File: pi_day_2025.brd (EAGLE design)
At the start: 50.8 x 25.4 mm, 98 parts, among them IC1 W25Q64JVXGIQ, J4 SM03B-SRSS-TB(LF)(SN), Q2 310mA/60V/1.6Ω, U1 APS6404L-3SQR-ZR, U2 RP2350A, U3 TPS76318DBVRG4, U4 TPS63001DRCR, U5 TXS0108EPWRG4, U6 LSM6DS3TR-C, U7 MCP73833T-AMI/MF, U8 TPS2113APWR, Y1 12MHz

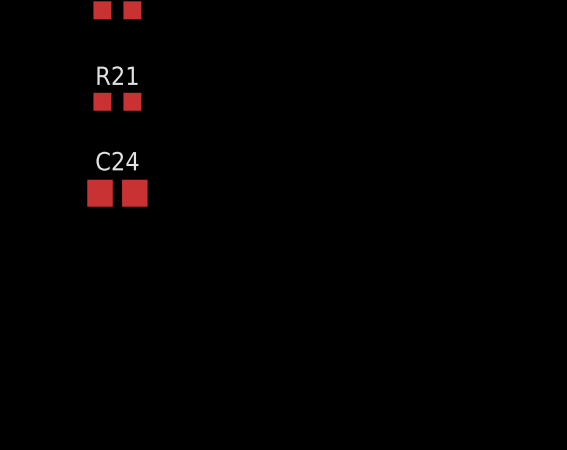
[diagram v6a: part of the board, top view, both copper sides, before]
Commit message: Added 1.8V regulator
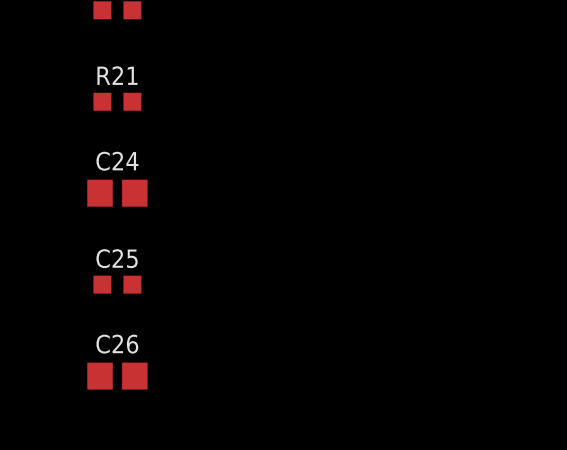
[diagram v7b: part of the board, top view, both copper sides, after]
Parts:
- added C25: 4.7uF, SparkFun-Capacitors:0402-TIGHT
- added C26: 1.0uF, SparkFun-Capacitors:0402
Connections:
- net 1.8V: now also C25.1, U3.5
- net 3.3V: now also C26.1, U3.1, U3.3
- net GND: now also C25.2, C26.2
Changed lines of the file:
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@@
 <attribute name="VALUE" x="-75.692" y="-283.718" size="0.6096" layer="27" font="vector" ratio="20" align="top-center"/>
+</element>
+<element name="C25" library="SparkFun-Capacitors" library_urn="urn:adsk.eagle:library:510" package="0402-TIGHT" package3d_urn="urn:adsk.eagle:package:41385069/1" value="4.7uF" x="-75.692" y="-286.004" smashed="yes">
+<attribute name="NAME" x="-75.692" y="-285.442" size="0.6096" layer="25" font="vector" ratio="20" align="bottom-center"/>
+<attribute name="PROD_ID" value="CAP-14240" x="-75.692" y="-286.004" size="1.778" layer="27" display="off"/>
+<attribute name="VALUE" x="-75.692" y="-286.566" size="0.6096" layer="27" font="vector" ratio="20" align="top-center"/>
+</element>
+<element name="C26" library="SparkFun-Capacitors" library_urn="urn:adsk.eagle:library:510" package="0402" package3d_urn="urn:adsk.eagle:package:41385089/1" value="1.0uF" x="-75.692" y="-289.052" smashed="yes">
+<attribute name="NAME" x="-75.692" y="-288.29" size="0.6096" layer="25" font="vector" ratio="20" align="bottom-center"/>
+<attribute name="PROD_ID" value="CAP-12417" x="-75.692" y="-289.052" size="1.778" layer="27" display="off"/>
+<attribute name="VALUE" x="-75.692" y="-289.814" size="0.6096" layer="27" font="vector" ratio="20" align="top-center"/>
 </element>
 </elements>
@@
 <contactref element="C23" pad="2"/>
 <contactref element="C24" pad="2"/>
+<contactref element="C25" pad="2"/>
+<contactref element="C26" pad="2"/>
 <wire x1="-47.991" y1="-197.104" x2="-50.978" y2="-197.997" width="0" layer="19" extent="1-1"/>
 <wire x1="-54.872" y1="-203.538" x2="-50.978" y2="-197.997" width="0" layer="19" extent="1-1"/>
@@
 <wire x1="-75.192" y1="-276.86" x2="-75.192" y2="-266.192" width="0" layer="19" extent="1-1"/>
 <wire x1="-75.112" y1="-282.956" x2="-75.192" y2="-276.86" width="0" layer="19" extent="1-1"/>
+<wire x1="-75.192" y1="-286.004" x2="-75.112" y2="-282.956" width="0" layer="19" extent="1-1"/>
+<wire x1="-75.112" y1="-289.052" x2="-75.192" y2="-286.004" width="0" layer="19" extent="1-1"/>
 <wire x1="-16.903" y1="-171.45" x2="-39.869" y2="-197.836" width="0" layer="19" extent="1-1"/>
 <wire x1="-17.708" y1="-157.48" x2="-16.903" y2="-171.45" width="0" layer="19" extent="1-1"/>
@@
 <contactref element="C21" pad="1"/>
 <contactref element="C22" pad="1"/>
-<wire x1="-54.022" y1="-203.188" x2="-35.462" y2="-198.374" width="0" layer="19" extent="1-1"/>
-<wire x1="-55.872" y1="-203.538" x2="-54.022" y2="-203.188" width="0" layer="19" extent="1-1"/>
-<wire x1="-56.722" y1="-201.688" x2="-55.872" y2="-203.538" width="0" layer="19" extent="1-1"/>
-<wire x1="-54.872" y1="-201.338" x2="-56.722" y2="-201.688" width="0" layer="19" extent="1-1"/>
+<contactref element="U3" pad="1"/>
+<contactref element="U3" pad="3"/>
+<contactref element="C26" pad="1"/>
+<wire x1="-47.991" y1="-198.054" x2="-47.991" y2="-196.154" width="0" layer="19" extent="1-1"/>
+<wire x1="-54.872" y1="-201.338" x2="-47.991" y2="-198.054" width="0" layer="19" extent="1-1"/>
+<wire x1="-56.722" y1="-201.688" x2="-54.872" y2="-201.338" width="0" layer="19" extent="1-1"/>
+<wire x1="-55.872" y1="-203.538" x2="-56.722" y2="-201.688" width="0" layer="19" extent="1-1"/>
+<wire x1="-54.022" y1="-203.188" x2="-55.872" y2="-203.538" width="0" layer="19" extent="1-1"/>
 <wire x1="-56.888" y1="-205.74" x2="-55.872" y2="-203.538" width="0" layer="19" extent="1-1"/>
 <wire x1="-59.56" y1="-202.962" x2="-56.722" y2="-201.688" width="0" layer="19" extent="1-1"/>
 <wire x1="-62.36" y1="-202.962" x2="-59.56" y2="-202.962" width="0" layer="19" extent="1-1"/>
+<wire x1="-35.462" y1="-198.374" x2="-47.991" y2="-198.054" width="0" layer="19" extent="1-1"/>
 <wire x1="-18.868" y1="-157.48" x2="-35.462" y2="-198.374" width="0" layer="19" extent="1-1"/>
 <wire x1="-12.132" y1="-150.126" x2="-18.868" y2="-157.48" width="0" layer="19" extent="1-1"/>
@@
 <wire x1="-76.192" y1="-263.144" x2="-56.888" y2="-205.74" width="0" layer="19" extent="1-1"/>
 <wire x1="-76.192" y1="-266.192" x2="-76.192" y2="-263.144" width="0" layer="19" extent="1-1"/>
+<wire x1="-76.272" y1="-289.052" x2="-76.192" y2="-266.192" width="0" layer="19" extent="1-1"/>
 </signal>
 <signal name="!RESET">
@@
 <signal name="1.8V">
 <contactref element="MK1" pad="1"/>
+<contactref element="U3" pad="5"/>
+<contactref element="C25" pad="1"/>
+<wire x1="-39.869" y1="-195.539" x2="-45.481" y2="-196.154" width="0" layer="19" extent="1-1"/>
+<wire x1="-76.192" y1="-286.004" x2="-45.481" y2="-196.154" width="0" layer="19" extent="1-1"/>
 </signal>
 <signal name="VCCA">

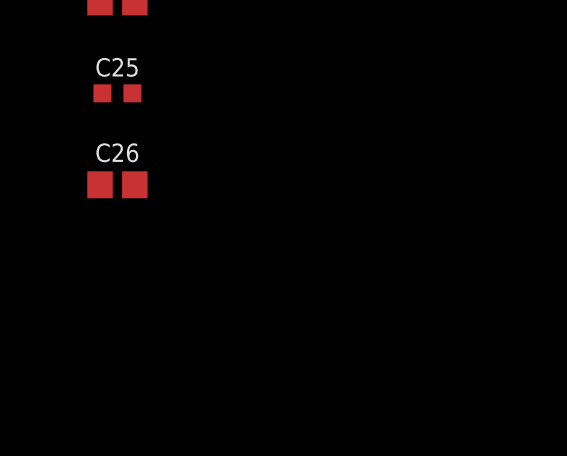
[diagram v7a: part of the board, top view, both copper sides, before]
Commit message: Added bypass capacitor to IA611
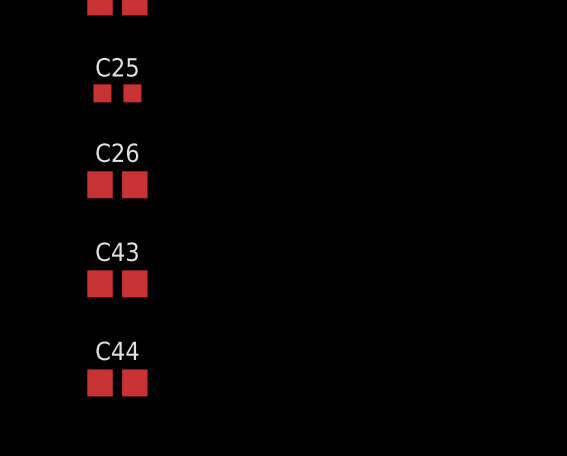
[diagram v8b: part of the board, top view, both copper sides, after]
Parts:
- added C43, C44: 1.0uF, SparkFun-Capacitors:0402
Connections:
- new net N$23: C44.1, MK1.2
- net 1.8V: now also C43.1
- net GND: now also C43.2, C44.2
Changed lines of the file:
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@@
 <attribute name="VALUE" x="-75.692" y="-289.814" size="0.6096" layer="27" font="vector" ratio="20" align="top-center"/>
+</element>
+<element name="C43" library="SparkFun-Capacitors" library_urn="urn:adsk.eagle:library:510" package="0402" package3d_urn="urn:adsk.eagle:package:41385089/1" value="1.0uF" x="-75.692" y="-292.354" smashed="yes">
+<attribute name="NAME" x="-75.692" y="-291.592" size="0.6096" layer="25" font="vector" ratio="20" align="bottom-center"/>
+<attribute name="PROD_ID" value="CAP-12417" x="-75.692" y="-292.354" size="1.778" layer="27" display="off"/>
+<attribute name="VALUE" x="-75.692" y="-293.116" size="0.6096" layer="27" font="vector" ratio="20" align="top-center"/>
+</element>
+<element name="C44" library="SparkFun-Capacitors" library_urn="urn:adsk.eagle:library:510" package="0402" package3d_urn="urn:adsk.eagle:package:41385089/1" value="1.0uF" x="-75.692" y="-295.656" smashed="yes">
+<attribute name="NAME" x="-75.692" y="-294.894" size="0.6096" layer="25" font="vector" ratio="20" align="bottom-center"/>
+<attribute name="PROD_ID" value="CAP-12417" x="-75.692" y="-295.656" size="1.778" layer="27" display="off"/>
+<attribute name="VALUE" x="-75.692" y="-296.418" size="0.6096" layer="27" font="vector" ratio="20" align="top-center"/>
 </element>
 </elements>
@@
 <contactref element="C25" pad="2"/>
 <contactref element="C26" pad="2"/>
+<contactref element="C43" pad="2"/>
+<contactref element="C44" pad="2"/>
 <wire x1="-47.991" y1="-197.104" x2="-50.978" y2="-197.997" width="0" layer="19" extent="1-1"/>
 <wire x1="-54.872" y1="-203.538" x2="-50.978" y2="-197.997" width="0" layer="19" extent="1-1"/>
@@
 <wire x1="-75.192" y1="-286.004" x2="-75.112" y2="-282.956" width="0" layer="19" extent="1-1"/>
 <wire x1="-75.112" y1="-289.052" x2="-75.192" y2="-286.004" width="0" layer="19" extent="1-1"/>
+<wire x1="-75.112" y1="-292.354" x2="-75.112" y2="-289.052" width="0" layer="19" extent="1-1"/>
+<wire x1="-75.112" y1="-295.656" x2="-75.112" y2="-292.354" width="0" layer="19" extent="1-1"/>
 <wire x1="-16.903" y1="-171.45" x2="-39.869" y2="-197.836" width="0" layer="19" extent="1-1"/>
 <wire x1="-17.708" y1="-157.48" x2="-16.903" y2="-171.45" width="0" layer="19" extent="1-1"/>
@@
 <contactref element="U3" pad="5"/>
 <contactref element="C25" pad="1"/>
+<contactref element="C43" pad="1"/>
 <wire x1="-39.869" y1="-195.539" x2="-45.481" y2="-196.154" width="0" layer="19" extent="1-1"/>
 <wire x1="-76.192" y1="-286.004" x2="-45.481" y2="-196.154" width="0" layer="19" extent="1-1"/>
+<wire x1="-76.272" y1="-292.354" x2="-76.192" y2="-286.004" width="0" layer="19" extent="1-1"/>
 </signal>
 <signal name="VCCA">
@@
 <wire x1="-59.56" y1="-203.962" x2="-59.56" y2="-204.462" width="0" layer="19" extent="1-1"/>
 </signal>
+<signal name="N$23">
+<contactref element="MK1" pad="2"/>
+<contactref element="C44" pad="1"/>
+<wire x1="-76.272" y1="-295.656" x2="-40.894" y2="-195.539" width="0" layer="19" extent="1-1"/>
+</signal>
 </signals>
